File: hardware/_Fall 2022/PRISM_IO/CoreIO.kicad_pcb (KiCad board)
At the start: 2 copper layers, 63.5 x 88.9 mm, 19 parts, among them J1 CORE_FC, J2 COTS_SWITCH_PLUG

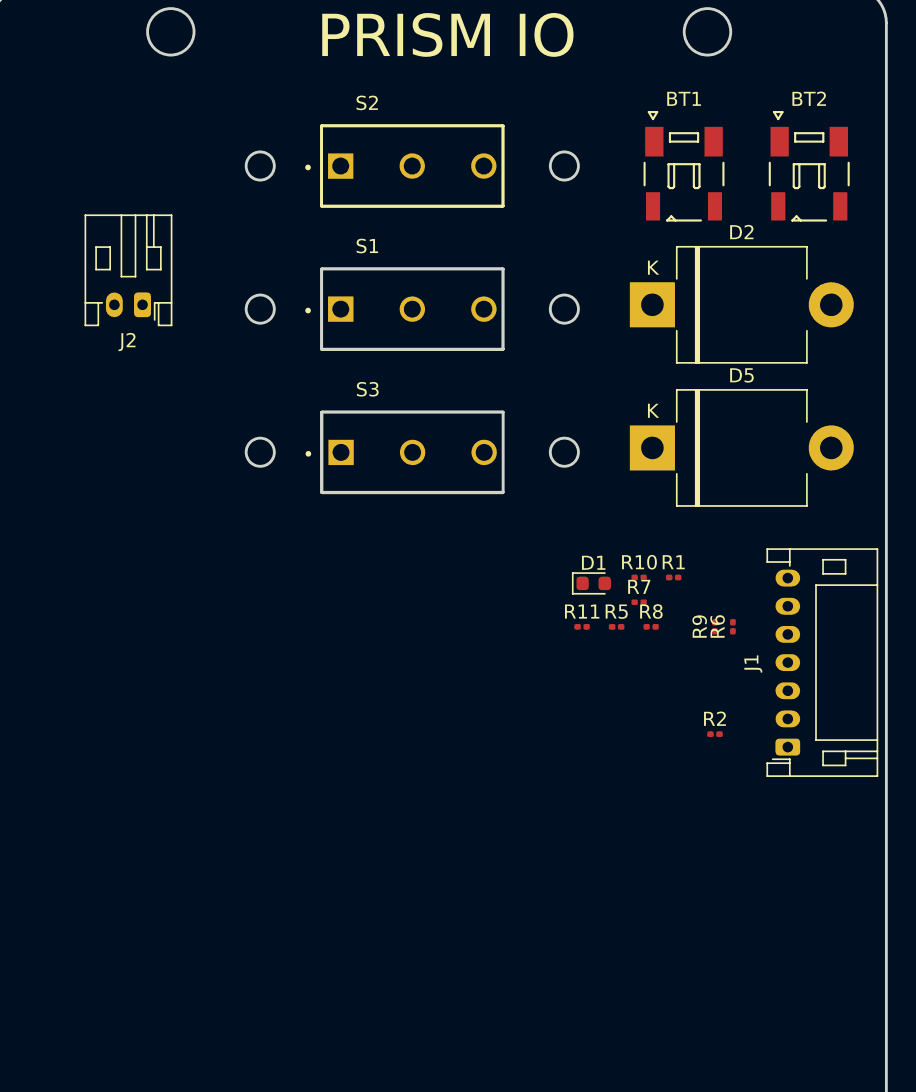
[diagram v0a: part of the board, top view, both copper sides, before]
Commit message: fixed some footprints on PRISM IO
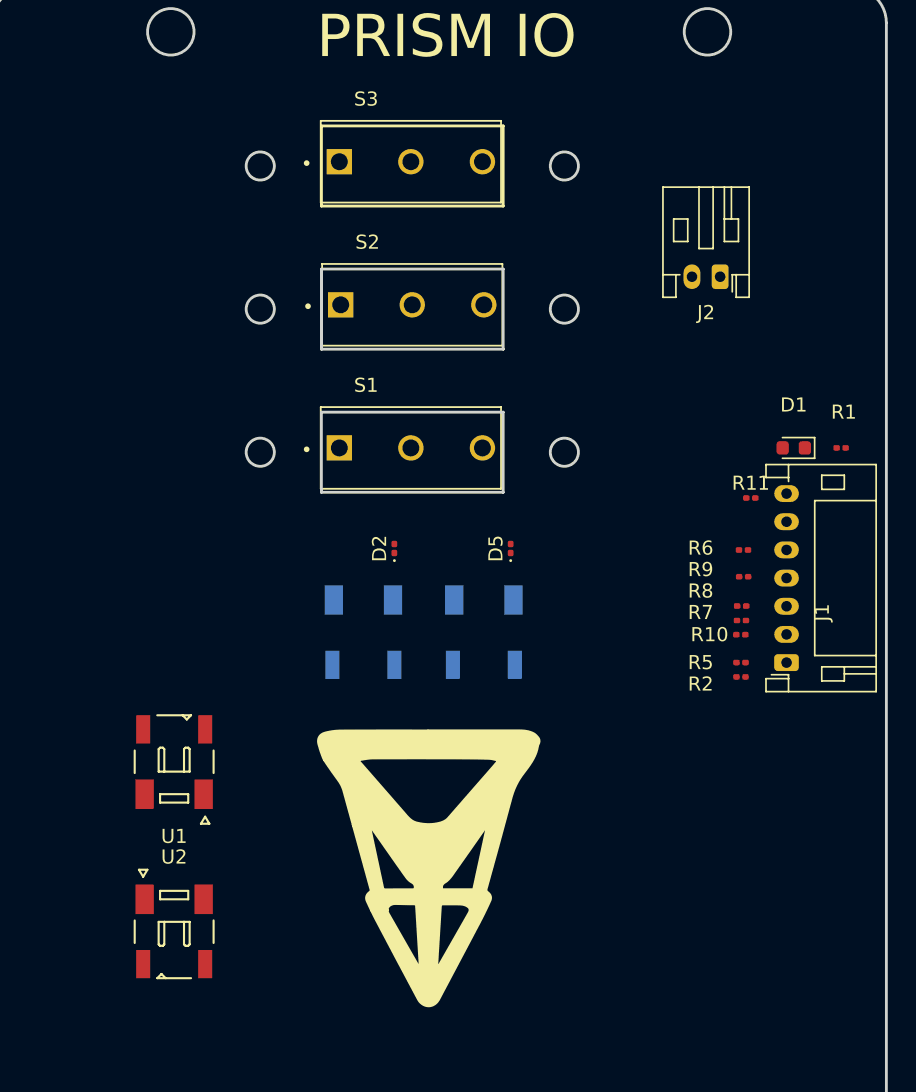
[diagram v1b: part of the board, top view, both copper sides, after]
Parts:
- added U1: PYRO 1, JST:JST_SFH_SM02B-SFHRS-TF_02x1.80mm_Angled, F.Cu at (124.2, 106.1)
- added U2: PYRO 2, JST:JST_SFH_SM02B-SFHRS-TF_02x1.80mm_Angled, F.Cu at (124.2, 118.2)
- BT1, BT2: moved to B.Cu
- D2, D5: footprint Diode_THT:D_5KPW_P12.70mm_Horizontal -> Diode_SMD:D_0201_0603Metric
- S1, S2, S3: footprint omron_D2F:SW_D2F-01F -> Sensors:SW_D2F-01F
- moved J2 41.1 mm to (162.9, 71.7)
- moved BT2 39.9 mm to (146.2, 96.9), turned to 180 degrees
- moved BT1 39.7 mm to (137.6, 96.9), turned to 180 degrees
- moved D2 25.2 mm to (139.8, 91.0), turned to 90 degrees
- moved S3 20.6 mm to (141.0, 63.5)
- moved D1 17.2 mm to (168.1, 83.8), turned to 180 degrees
- moved R11 15.1 mm to (165.1, 87.4)
- moved R1 15.0 mm to (171.5, 83.8), turned to 180 degrees
- moved D5 12.3 mm to (148.1, 91.0), turned to 90 degrees
- moved S1 9.85 mm to (141.0, 83.8)
- moved S2 9.85 mm to (141.1, 73.7)
- moved R5 9.19 mm to (164.4, 99.1)
- moved R10 8.28 mm to (164.4, 97.1)
- moved R7 7.38 mm to (164.4, 96.1)
- moved R8 6.60 mm to (164.5, 95.0), turned to 180 degrees
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
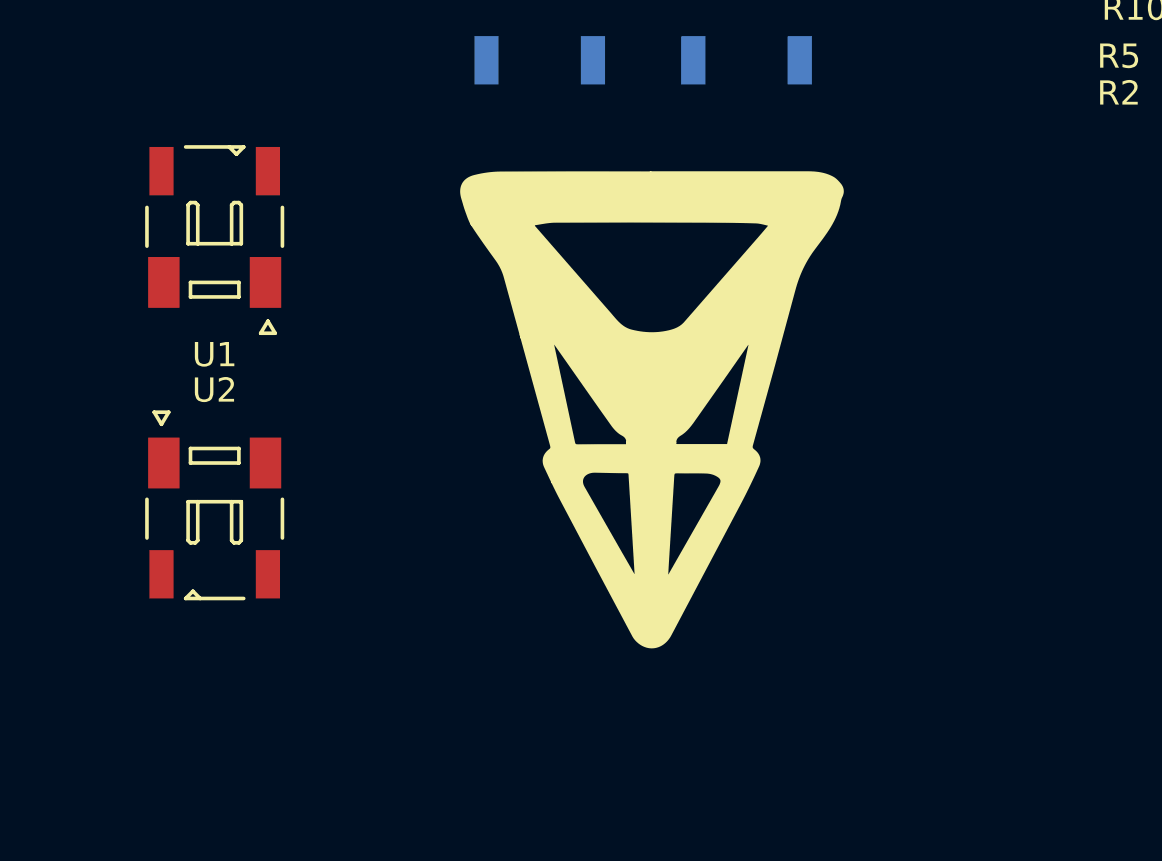
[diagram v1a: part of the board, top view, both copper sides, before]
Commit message: Update CoreIO.kicad_pcb
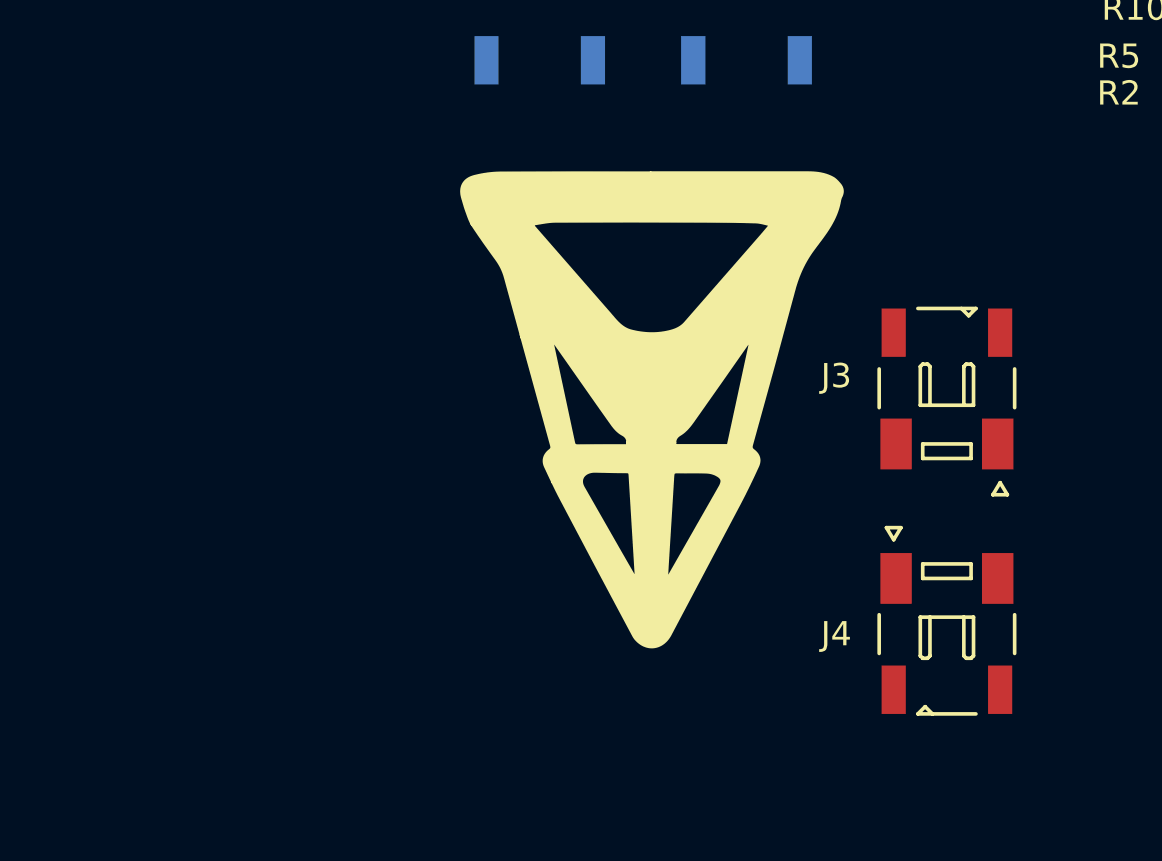
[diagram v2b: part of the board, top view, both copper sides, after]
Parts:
- removed U1: PYRO 1, JST:JST_SFH_SM02B-SFHRS-TF_02x1.80mm_Angled
- removed U2: PYRO 2, JST:JST_SFH_SM02B-SFHRS-TF_02x1.80mm_Angled
- added J3: PYRO 1, JST:JST_SFH_SM02B-SFHRS-TF_02x1.80mm_Angled, F.Cu at (154.4, 112.8)
- added J4: PYRO 2, JST:JST_SFH_SM02B-SFHRS-TF_02x1.80mm_Angled, F.Cu at (154.4, 122.9)

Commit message: add footprint for diode
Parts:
- removed D5: D_Schottky, Diode_SMD:D_0201_0603Metric
- added D3: SS54, JLC_footprints:DO-214AC, F.Cu at (146.3, 90.9)
- added JP1: Jumper, Jumper:SolderJumper-3_P1.3mm_Open_Pad1.0x1.5mm_NumberLabels, F.Cu at (156.0, 84.3)
- added JP2: Jumper, Jumper:SolderJumper-3_P1.3mm_Open_Pad1.0x1.5mm_NumberLabels, F.Cu at (156.0, 74.2)
- added JP3: Jumper, Jumper:SolderJumper-3_P1.3mm_Open_Pad1.0x1.5mm_NumberLabels, F.Cu at (156.0, 64.0)
- D2: value D_Schottky -> SS54; footprint Diode_SMD:D_0201_0603Metric -> JLC_footprints:DO-214AC
- S1: value D2F-01F -> POWER
- S2: value D2F-01F -> ARM
- S3: value COTS_SWITCH -> COTS
- moved J2 5.21 mm to (168.1, 71.5)
- moved D2 2.13 mm to (137.7, 90.9), turned to 0 degrees
- moved S3 0.51 mm to (141.1, 64.0)
- moved S2 0.25 mm to (141.1, 73.9)
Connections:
- S1 pad 2: unconnected-(S1-Pad2) -> Net-(JP1-Pad1)
- S1 pad 3: /VBAT -> Net-(JP1-Pad3)
- S2 pad 2: unconnected-(S2-Pad2) -> Net-(JP2-Pad1)
- S2 pad 3: unconnected-(S2-Pad3) -> Net-(JP2-Pad3)
- S3 pad 2: unconnected-(S3-Pad2) -> Net-(JP3-Pad1)
- S3 pad 3: Net-(J2-Pad1) -> Net-(JP3-Pad3)

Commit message: update core IO with minor changes
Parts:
- R6, R9: value 10k -> 1M
- moved S1 0.66 mm to (141.3, 84.4)
- moved S3 0.31 mm to (141.2, 63.7)
- moved S2 0.20 mm to (141.2, 74.0)
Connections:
- D1 pad 2: /VBAT -> /V_BATT
- J1 pad 1: /ARM -> GND
- J1 pad 2: /CONT 2 -> /V_BATT
- J1 pad 3: /CONT 1 -> /PYRO 1
- J1 pad 5: /PYRO 1 -> /ARM
- J1 pad 6: /VBAT -> /CONT 1
- J1 pad 7: GND -> /CONT 2
- JP1 pad 2: /VBAT -> /V_BATT
- S2 pad 1: /VBAT -> /V_BATT
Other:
- outline, holes or cut-outs redrawn

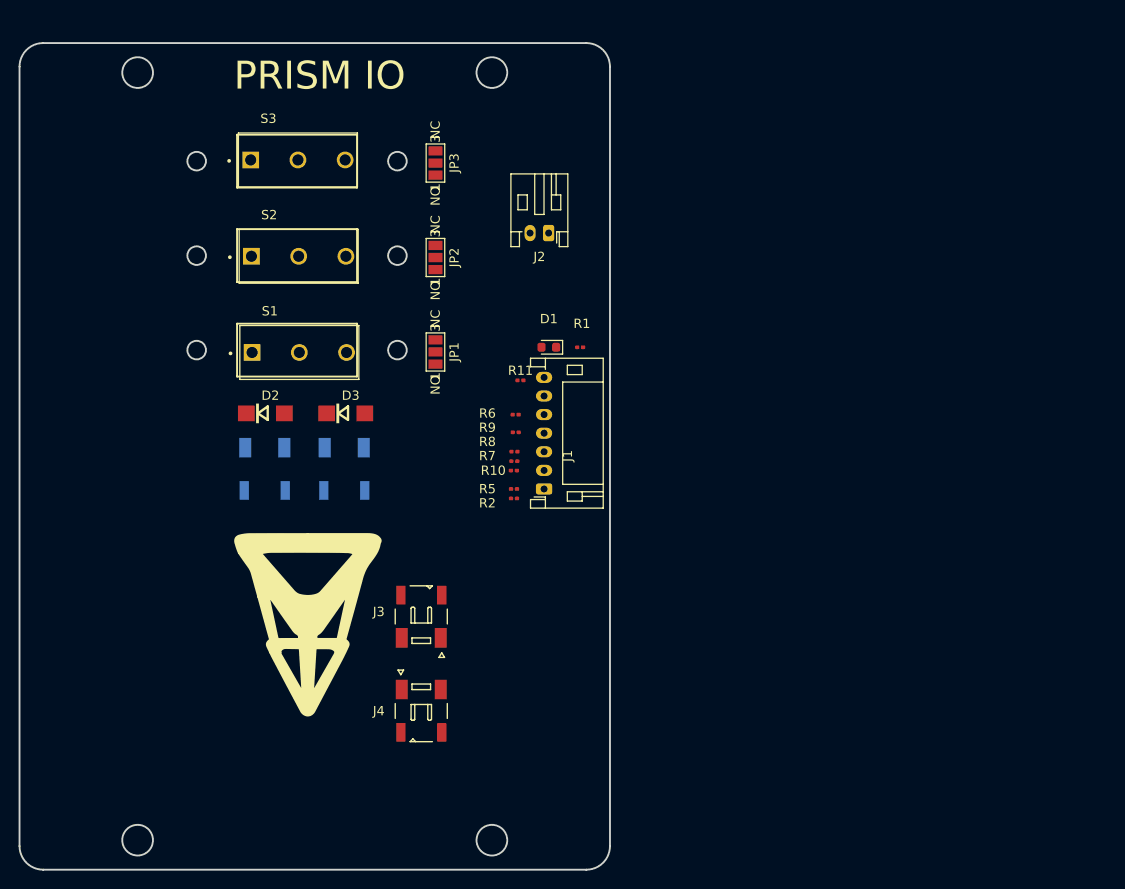
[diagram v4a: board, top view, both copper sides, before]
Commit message: new dxf for prism io
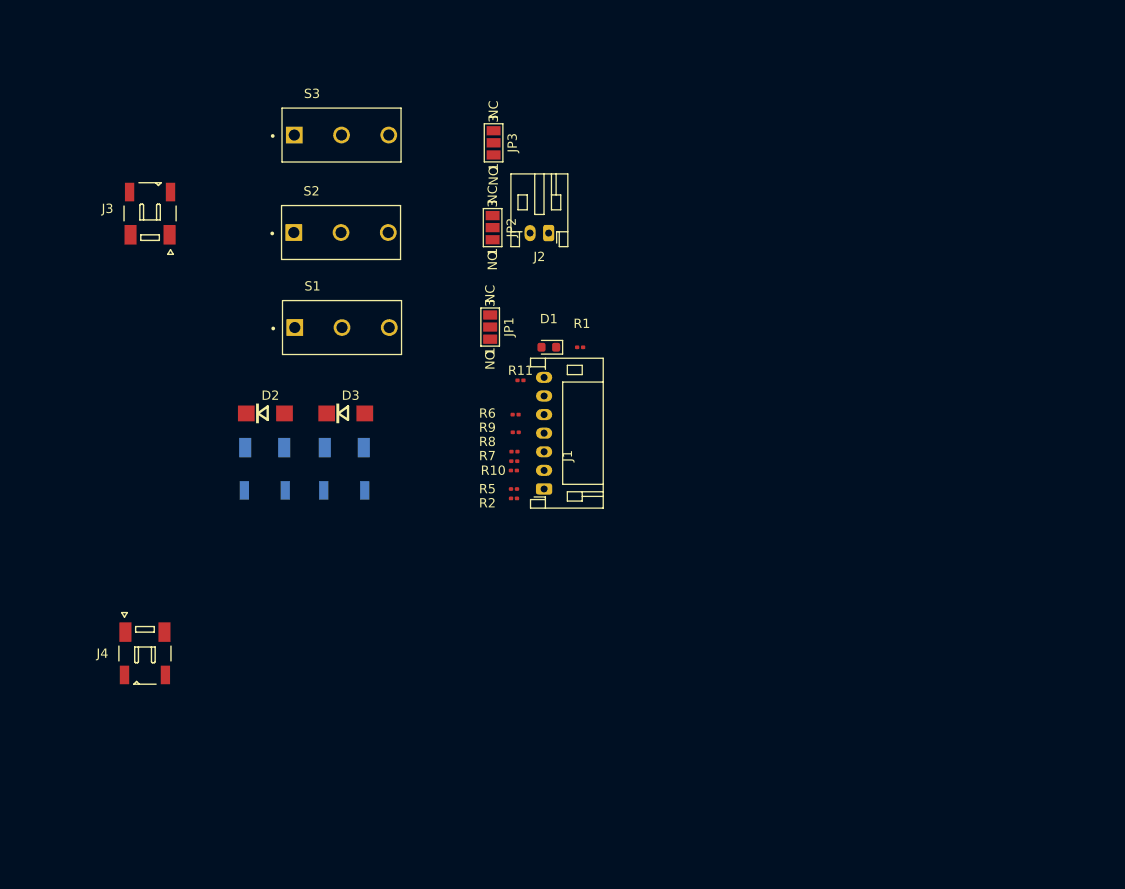
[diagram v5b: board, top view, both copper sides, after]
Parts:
- moved J3 52.2 mm to (125.3, 69.4)
- moved J4 30.4 mm to (124.7, 116.8)
- moved JP2 6.94 mm to (162.1, 71.0)
- moved JP3 6.62 mm to (162.2, 61.8)
- moved JP1 6.47 mm to (161.8, 81.6)
- moved S3 5.40 mm to (145.9, 61.0)
- moved S1 5.32 mm to (145.9, 81.7)
- moved S2 5.22 mm to (145.8, 71.5)
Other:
- board outline removed
- board text removed: "PRISM IO"

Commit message: add cad models
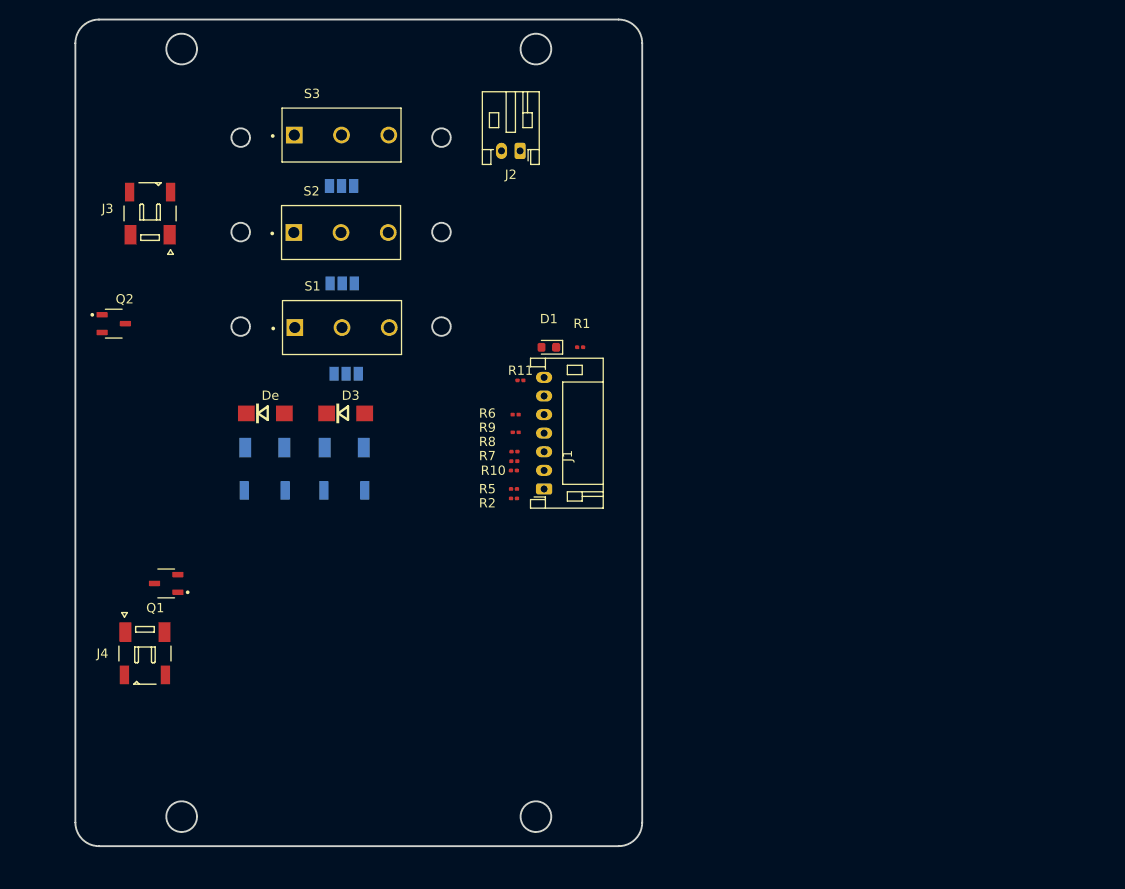
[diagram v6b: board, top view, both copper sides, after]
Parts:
- added Q1: AO3400A, AO3400A:SOT95P280X125-3N, F.Cu at (127.0, 109.2)
- added Q2: AO3400A, AO3400A:SOT95P280X125-3N, F.Cu at (121.4, 81.3)
- JP1, JP2, JP3: moved to B.Cu
- moved JP2 17.3 mm to (145.9, 77.0), turned to 0 degrees
- moved JP3 17.0 mm to (145.9, 66.5), turned to 0 degrees
- moved JP1 16.3 mm to (146.4, 86.7), turned to 0 degrees
- moved J2 9.36 mm to (165.1, 62.7)
- renumbered D2 to De
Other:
- board outline added: 61 x 88.9 mm

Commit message: logos
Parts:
- added ?: LOGO, LOGO, F.Cu at (148.6, 134.6)
- added ?: LOGO, LOGO, F.Cu at (148.1, 53.9)
- added G***: LOGO, LOGO, F.Cu at (147.3, 111.8)
- moved J1 1.93 mm to (167.8, 101.0)
- moved JP2 1.93 mm to (146.1, 78.9)
- moved R1 1.93 mm to (171.7, 85.7)
- moved R6 1.93 mm to (164.7, 93.0)
- moved D1 1.93 mm to (168.3, 85.7)
- moved D3 1.93 mm to (146.4, 92.9)
- moved De 1.93 mm to (137.8, 92.9)
- moved J3 1.93 mm to (125.4, 71.3)
- moved J4 1.93 mm to (124.9, 118.7)
- moved JP1 1.93 mm to (146.5, 88.6)
- moved Q1 1.93 mm to (127.1, 111.1)
- moved Q2 1.93 mm to (121.5, 83.2)
- moved R10 1.93 mm to (164.5, 99.0)
- moved R11 1.93 mm to (165.2, 89.3)
- moved R2 1.93 mm to (164.5, 102.0)
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
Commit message: io layout
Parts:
- moved G*** 67.3 mm to (214.6, 113.0)
- moved Q2 50.2 mm to (170.2, 71.1), turned to 90 degrees
- moved J4 48.3 mm to (172.7, 125.1)
- moved J3 47.8 mm to (172.7, 64.8)
- moved Q1 44.6 mm to (171.4, 116.2), turned to -90 degrees
- moved J2 41.1 mm to (124.2, 67.2)
- moved BT2 11.2 mm to (157.5, 99.1)
- moved D3 11.1 mm to (157.5, 92.1)
- moved BT1 10.9 mm to (148.6, 99.1)
- moved D2 10.8 mm to (148.6, 92.1), turned to 180 degrees
- moved R10 9.46 mm to (164.5, 89.5)
- moved R2 8.65 mm to (164.5, 93.3)
- moved R7 7.19 mm to (164.5, 90.8)
- moved R5 7.00 mm to (164.5, 94.0)
- moved JP2 5.80 mm to (143.5, 73.7), turned to 180 degrees
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- renumbered De to D2
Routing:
- added copper zone on B.Cu, net GND
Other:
- outline, holes or cut-outs redrawn
